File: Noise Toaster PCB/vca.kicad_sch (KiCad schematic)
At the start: 7 parts, among them Q7 2N5457, X12 Conn_01x01_Pin, X13 Conn_01x01_Pin

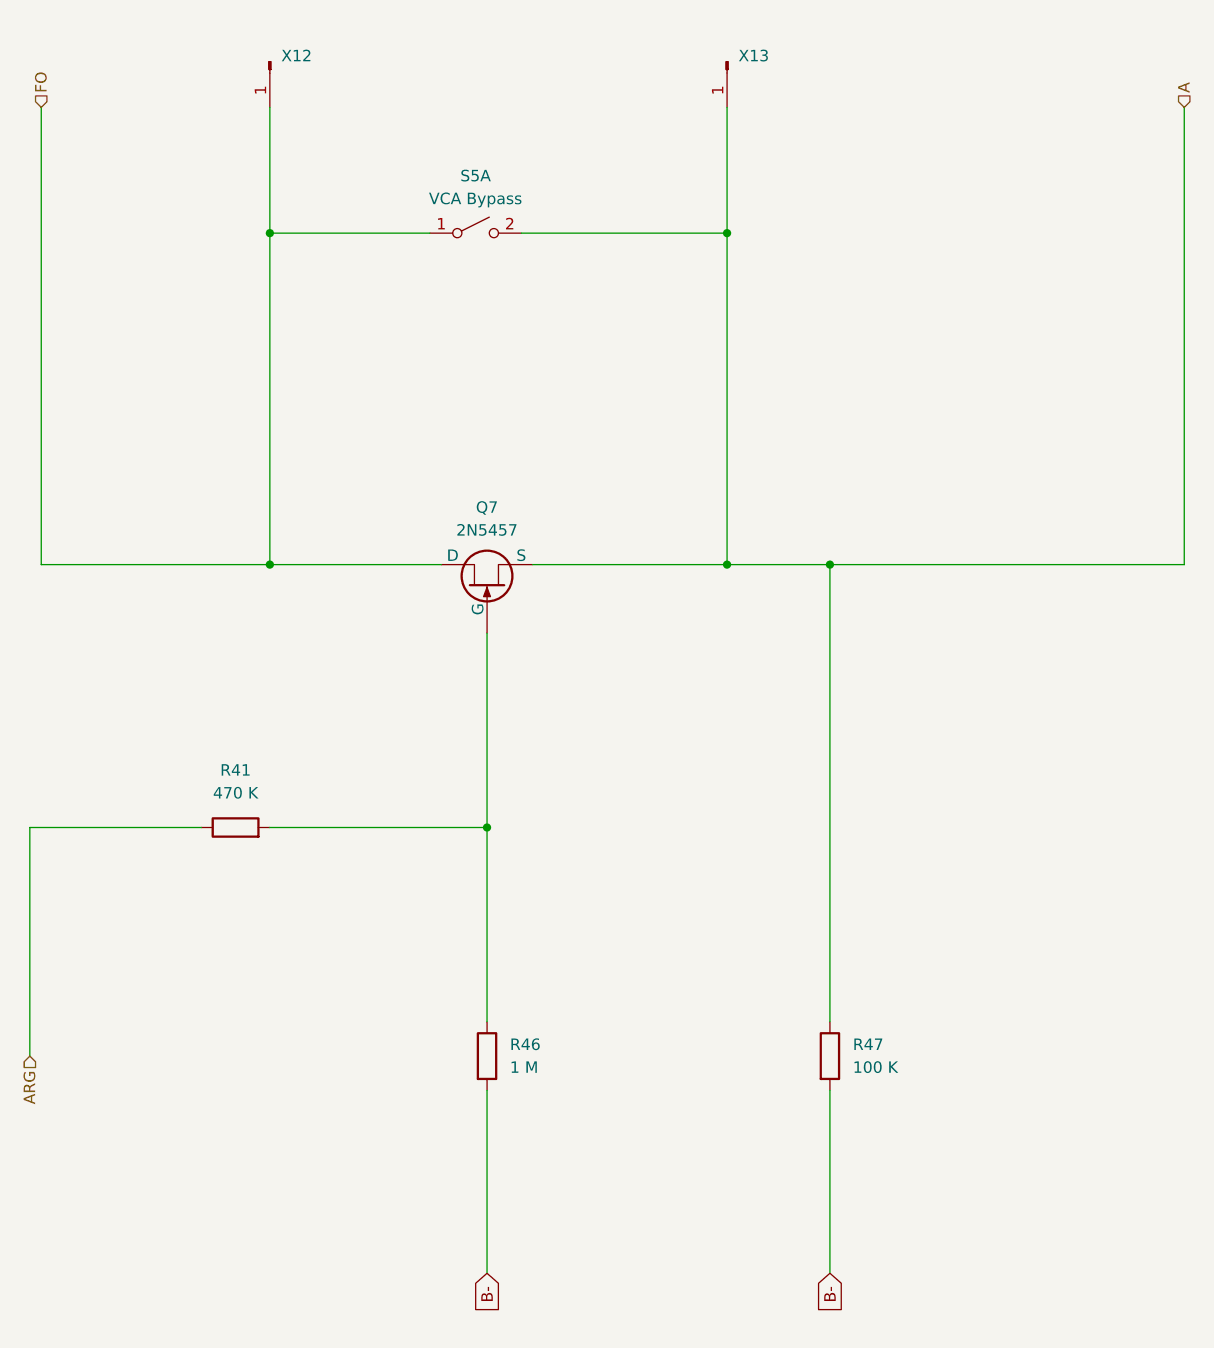
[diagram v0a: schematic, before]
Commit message: updated schematics
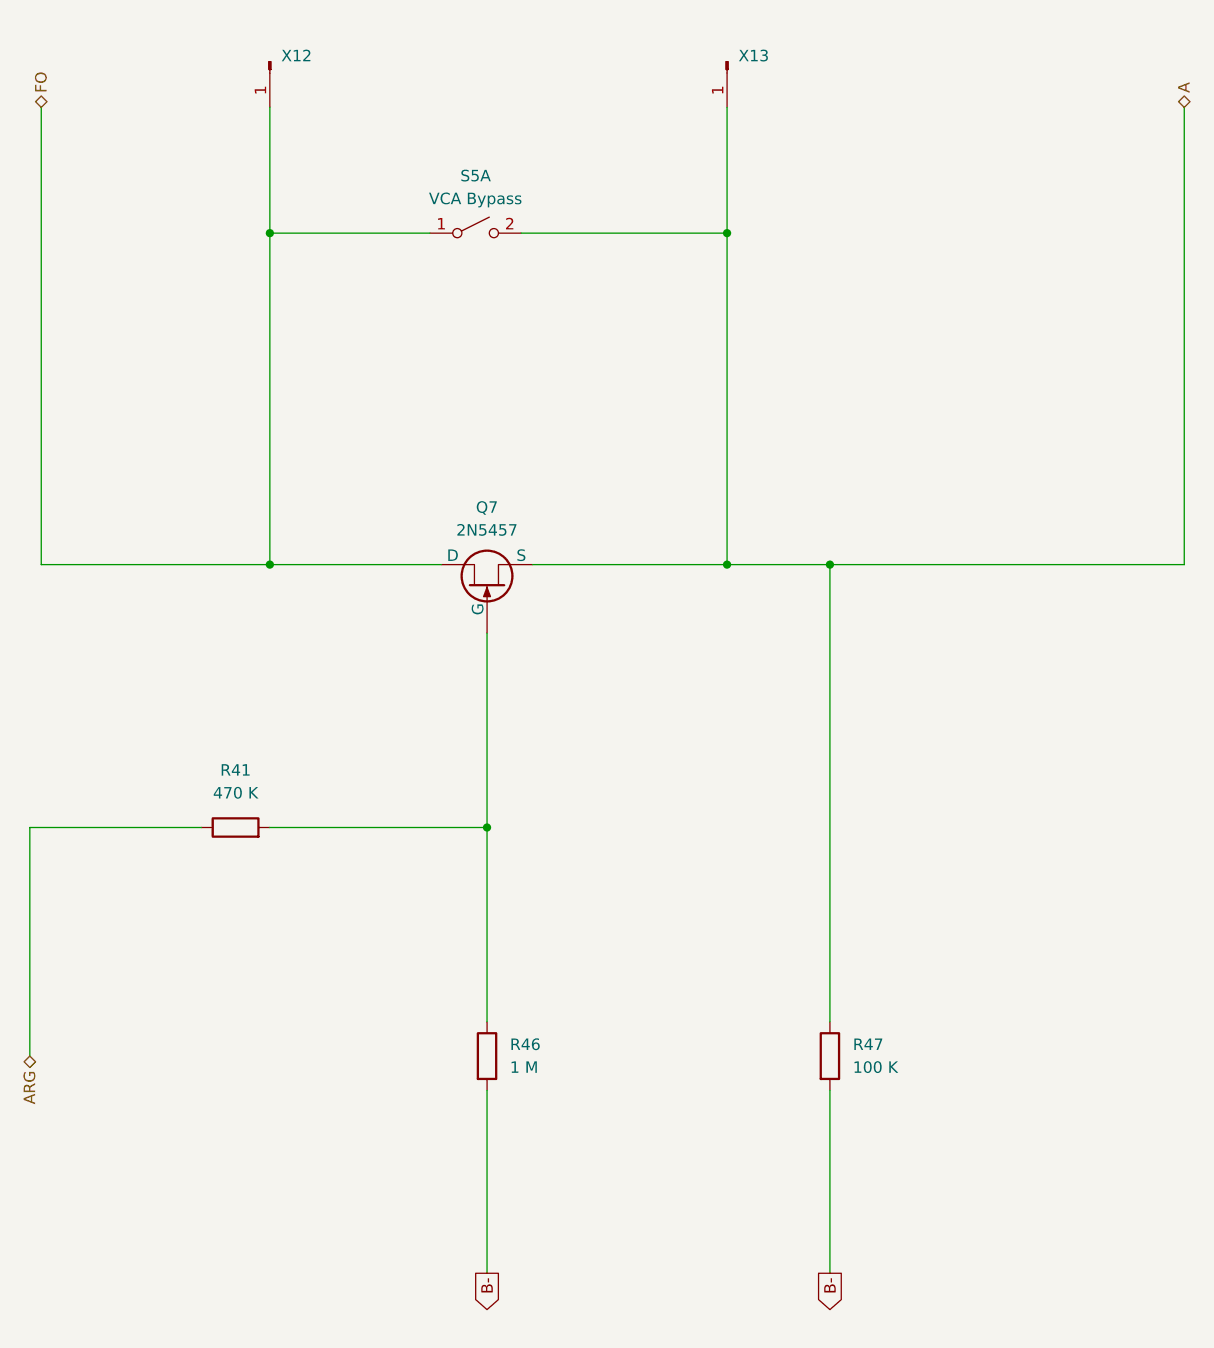
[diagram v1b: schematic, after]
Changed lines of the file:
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@@
     (stroke (width 0) (type default))
   )
-  (global_label "B-" (shape input) (at 113.03 166.37 270) (fields_autoplaced)
+  (global_label "B-" (shape output) (at 113.03 166.37 270) (fields_autoplaced)
     (effects (font (size 1.27 1.27)) (justify right))
     (property "Intersheetrefs" "${INTERSHEET_REFS}" (at 113.03 172.1976 90)
@@
     )
   )
-  (global_label "B-" (shape input) (at 151.13 166.37 270) (fields_autoplaced)
+  (global_label "B-" (shape output) (at 151.13 166.37 270) (fields_autoplaced)
     (effects (font (size 1.27 1.27)) (justify right))
     (property "Intersheetrefs" "${INTERSHEET_REFS}" (at 151.13 172.1976 90)
@@
     )
   )
-  (hierarchical_label "ARG" (shape input) (at 62.23 142.24 270) (fields_autoplaced)
+  (hierarchical_label "ARG" (shape bidirectional) (at 62.23 142.24 270) (fields_autoplaced)
     (effects (font (size 1.27 1.27)) (justify right))
   )
-  (hierarchical_label "FO" (shape input) (at 63.5 36.83 90) (fields_autoplaced)
+  (hierarchical_label "FO" (shape bidirectional) (at 63.5 36.83 90) (fields_autoplaced)
     (effects (font (size 1.27 1.27)) (justify left))
   )
-  (hierarchical_label "A" (shape input) (at 190.5 36.83 90) (fields_autoplaced)
+  (hierarchical_label "A" (shape bidirectional) (at 190.5 36.83 90) (fields_autoplaced)
     (effects (font (size 1.27 1.27)) (justify left))
   )

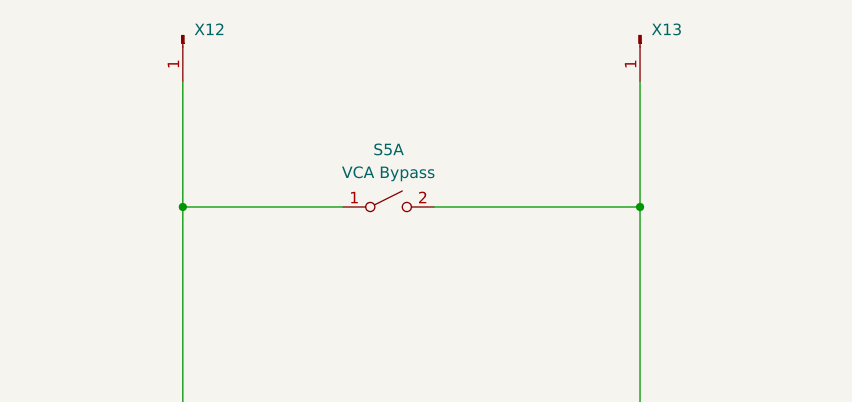
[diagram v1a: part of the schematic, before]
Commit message: refactored the schematic
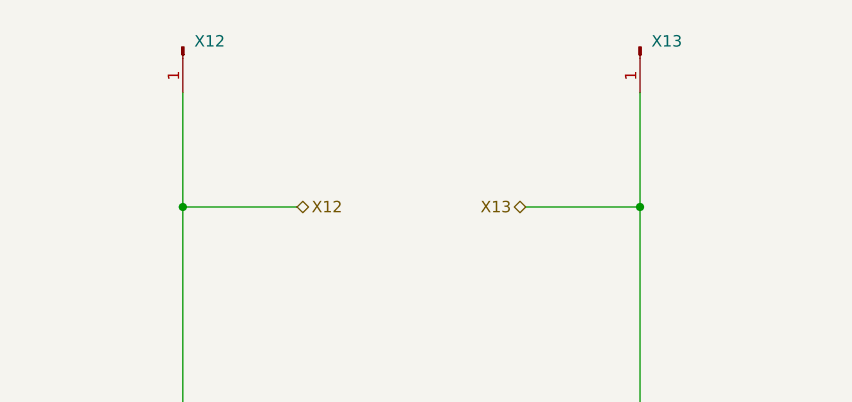
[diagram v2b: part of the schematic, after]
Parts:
- removed S5: VCA Bypass, symbol Switch:SW_DPST_x2
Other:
- moved on the sheet: X12, X13
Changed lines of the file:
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@@
     (comment 3 "Music From Outer Space LLC")
   )
+  (junction (at 139.7 50.8) (diameter 0) (color 0 0 0 0)
+  )
   (junction (at 139.7 87.63) (diameter 0) (color 0 0 0 0)
+  )
+  (junction (at 88.9 50.8) (diameter 0) (color 0 0 0 0)
   )
   (junction (at 151.13 87.63) (diameter 0) (color 0 0 0 0)
@@
   (junction (at 88.9 87.63) (diameter 0) (color 0 0 0 0)
   )
-  (junction (at 88.9 50.8) (diameter 0) (color 0 0 0 0)
-  )
-  (junction (at 139.7 50.8) (diameter 0) (color 0 0 0 0)
-  )
   (junction (at 113.03 116.84) (diameter 0) (color 0 0 0 0)
   )
-  (wire (pts (xy 106.68 50.8) (xy 88.9 50.8))
+  (wire (pts (xy 139.7 50.8) (xy 139.7 87.63))
+    (stroke (width 0) (type default))
+  )
+  (wire (pts (xy 127 50.8) (xy 139.7 50.8))
+    (stroke (width 0) (type default))
+  )
+  (wire (pts (xy 88.9 50.8) (xy 101.6 50.8))
     (stroke (width 0) (type default))
   )
@@
     (stroke (width 0) (type default))
   )
-  (wire (pts (xy 88.9 50.8) (xy 88.9 87.63))
-    (stroke (width 0) (type default))
-  )
-  (wire (pts (xy 88.9 36.83) (xy 88.9 50.8))
+  (wire (pts (xy 88.9 38.1) (xy 88.9 50.8))
     (stroke (width 0) (type default))
   )
@@
     (stroke (width 0) (type default))
   )
-  (wire (pts (xy 139.7 50.8) (xy 139.7 87.63))
+  (wire (pts (xy 139.7 38.1) (xy 139.7 50.8))
     (stroke (width 0) (type default))
   )
@@
     (stroke (width 0) (type default))
   )
-  (wire (pts (xy 139.7 36.83) (xy 139.7 50.8))
-    (stroke (width 0) (type default))
-  )
   (wire (pts (xy 151.13 87.63) (xy 139.7 87.63))
     (stroke (width 0) (type default))
   )
-  (wire (pts (xy 116.84 50.8) (xy 139.7 50.8))
+  (wire (pts (xy 88.9 50.8) (xy 88.9 87.63))
     (stroke (width 0) (type default))
   )
@@
     )
   )
+  (hierarchical_label "X13" (shape bidirectional) (at 127 50.8 180) (fields_autoplaced)
+    (effects (font (size 1.27 1.27)) (justify right))
+  )
   (hierarchical_label "ARG" (shape bidirectional) (at 62.23 142.24 270) (fields_autoplaced)
     (effects (font (size 1.27 1.27)) (justify right))
   )
   (hierarchical_label "FO" (shape bidirectional) (at 63.5 36.83 90) (fields_autoplaced)
+    (effects (font (size 1.27 1.27)) (justify left))
+  )
+  (hierarchical_label "X12" (shape bidirectional) (at 101.6 50.8 0) (fields_autoplaced)
     (effects (font (size 1.27 1.27)) (justify left))
   )
@@
     )
   )
-  (symbol (lib_id "Switch:SW_DPST_x2") (at 111.76 50.8 0) (unit 1)
-    (in_bom yes) (on_board yes) (dnp no) (fields_autoplaced)
-    (property "Reference" "S5" (at 111.76 44.45 0)
-      (effects (font (size 1.27 1.27)))
-    )
-    (property "Value" "VCA Bypass" (at 111.76 46.99 0)
-      (effects (font (size 1.27 1.27)))
-    )
-    (property "Footprint" "" (at 111.76 50.8 0)
-      (effects (font (size 1.27 1.27)) hide)
-    )
-    (property "Datasheet" "~" (at 111.76 50.8 0)
-      (effects (font (size 1.27 1.27)) hide)
-    )
-    (pin "1")
-    (pin "2")
-    (pin "3")
-    (pin "4")
-    (instances
-      (project "Noise Toaster PCB"
-        (path "/7be3f398-d902-4566-9ee4-0bff072cd47e/6dd5f5bc-1b9c-4908-9997-3d64c0cf1aef"
-          (reference "S5") (unit 1)
-        )
-      )
-    )
-  )
   (symbol (lib_id "Device:R") (at 151.13 142.24 0) (unit 1)
     (in_bom yes) (on_board yes) (dnp no) (fields_autoplaced)
@@
     )
   )
-  (symbol (lib_id "Connector:Conn_01x01_Pin") (at 139.7 31.75 270) (unit 1)
+  (symbol (lib_id "Connector:Conn_01x01_Pin") (at 139.7 33.02 270) (unit 1)
     (in_bom yes) (on_board yes) (dnp no) (fields_autoplaced)
-    (property "Reference" "X13" (at 140.97 31.115 90)
+    (property "Reference" "X13" (at 140.97 32.385 90)
       (effects (font (size 1.27 1.27)) (justify left))
     )
-    (property "Value" "Conn_01x01_Pin" (at 140.97 33.655 90)
+    (property "Value" "Conn_01x01_Pin" (at 140.97 34.925 90)
       (effects (font (size 1.27 1.27)) (justify left) hide)
     )
-    (property "Footprint" "" (at 139.7 31.75 0)
+    (property "Footprint" "" (at 139.7 33.02 0)
       (effects (font (size 1.27 1.27)) hide)
     )
-    (property "Datasheet" "~" (at 139.7 31.75 0)
+    (property "Datasheet" "~" (at 139.7 33.02 0)
       (effects (font (size 1.27 1.27)) hide)
     )
@@
     )
   )
-  (symbol (lib_id "Connector:Conn_01x01_Pin") (at 88.9 31.75 270) (unit 1)
+  (symbol (lib_id "Connector:Conn_01x01_Pin") (at 88.9 33.02 270) (unit 1)
     (in_bom yes) (on_board yes) (dnp no) (fields_autoplaced)
-    (property "Reference" "X12" (at 90.17 31.115 90)
+    (property "Reference" "X12" (at 90.17 32.385 90)
       (effects (font (size 1.27 1.27)) (justify left))
     )
-    (property "Value" "Conn_01x01_Pin" (at 90.17 33.655 90)
+    (property "Value" "Conn_01x01_Pin" (at 90.17 34.925 90)
       (effects (font (size 1.27 1.27)) (justify left) hide)
     )
-    (property "Footprint" "" (at 88.9 31.75 0)
+    (property "Footprint" "" (at 88.9 33.02 0)
       (effects (font (size 1.27 1.27)) hide)
     )
-    (property "Datasheet" "~" (at 88.9 31.75 0)
+    (property "Datasheet" "~" (at 88.9 33.02 0)
       (effects (font (size 1.27 1.27)) hide)
     )
